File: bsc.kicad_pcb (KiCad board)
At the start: 4 copper layers, 120 x 100 mm, 278 parts, among them IC1 ILD217T, IC2 ILD217T, IC3 ILD217T, J1 Conn_JTAG_ESP, J10 JP_REL1_COM_12V, J12 JP_REL2_COM_12V, J13 JP_REL3_COM_12V, J14 Conn_REL1, J15 Conn_REL2, J16 Conn_REL3, J2 Prog, J3 Conn_Extension, J4 Boot, J5 JP_REL4_COM_12V, J6 JP_U3TX_EN, J8 JP_REL5_COM_12V, J9 JP_REL6_COM_12V, K2 TIANBO-HJR-4102-L, K3 TIANBO-HJR-4102-L, K4 TIANBO-HJR-4102-L, K5 TIANBO-HJR-4102-L, K6 TIANBO-HJR-4102-L, K7 TIANBO-HJR-4102-L, Q1 BC857BS, Q10 BC846, Q11 BC846, Q12 IRLML2244, Q13 BC857BS, Q14 IRLML2244, Q2 BSS138, Q3 BSS138, Q4 BSS138, Q5 BSS138, Q6 BSS138, Q7 BSS138, Q8 BC846, Q9 BC846, U1 LMO78_03-0.5, U10 74HC595, U11 74HC14, U12 74HC165, U13 ADuM1201AR, U16 SP3485EN, U19 LMO78_05-0.5, U2 ESP32WROOM32E16, U20 HC 151, U3 ADM2483xRW, U4 ADuM1201AR, U6 ADuM1201AR, U7 SN65HVD234, U8 SP3485EN, X1 Conn_S2, X2 Conn_S1, X3 Conn_DI, X4 Conn_SV, X5 Conn_Rel2, X6 Conn_Rel1

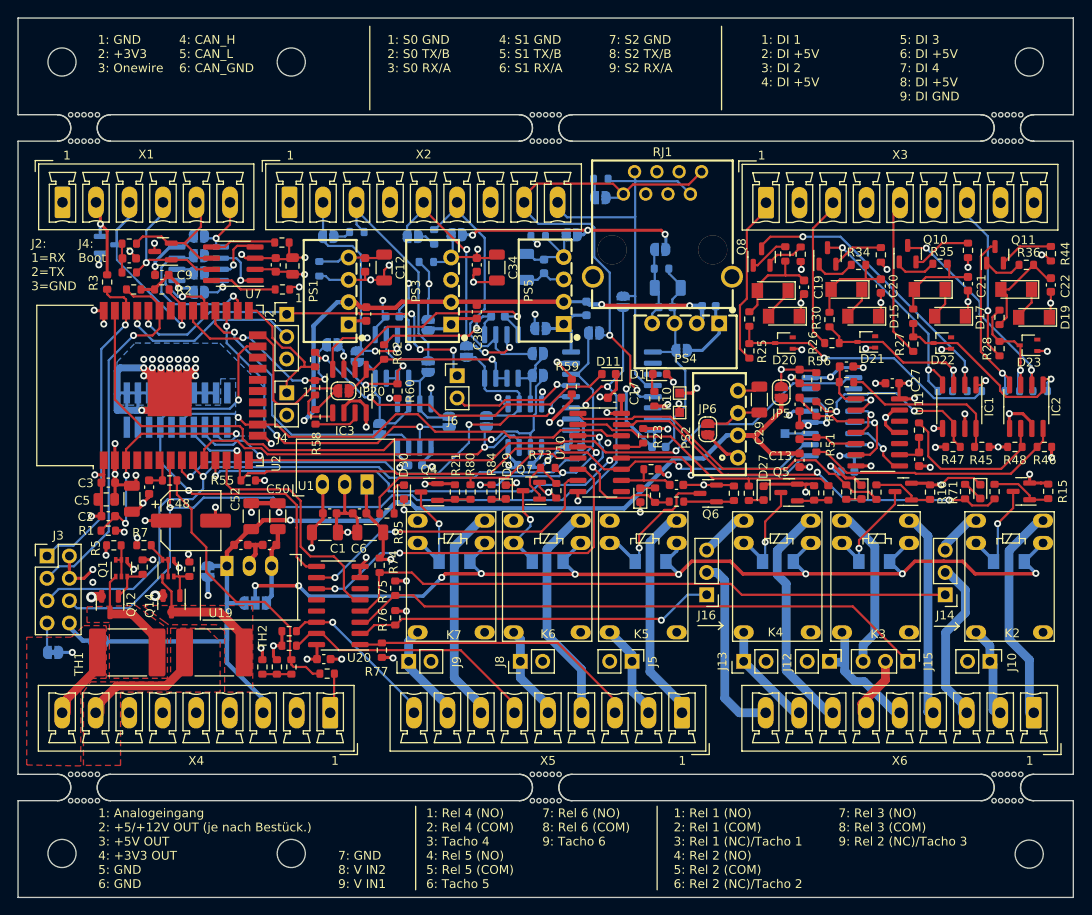
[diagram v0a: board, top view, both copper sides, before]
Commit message: Improvements added (Ref 2.4.1)
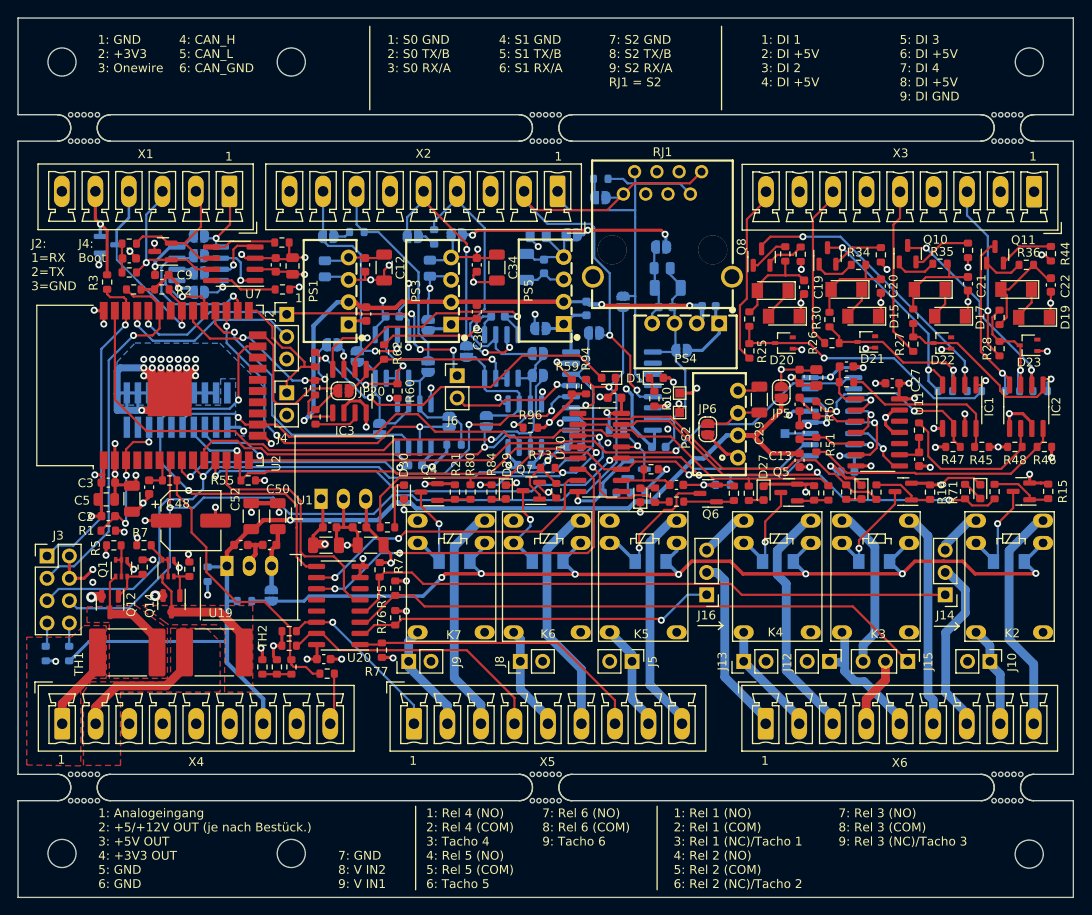
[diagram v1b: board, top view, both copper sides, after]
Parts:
- removed JP28: 12V_5V, Jumper:SolderJumper-2_P1.3mm_Bridged_RoundedPad1.0x1.5mm
- removed JP29: JP_REL_VCC, Jumper:SolderJumper-3_P1.3mm_Bridged12_RoundedPad1.0x1.5mm_NumberLabels
- removed JP30: JP_EXT_5V, Jumper:SolderJumper-2_P1.3mm_Bridged_RoundedPad1.0x1.5mm
- removed JP31: JP_EXT_3V3, Jumper:SolderJumper-2_P1.3mm_Bridged_RoundedPad1.0x1.5mm
- added C36: 10uF, Capacitor_SMD:C_0603_1608Metric, B.Cu at (97.3, 70.0)
- added JP25: REL_VIN, Jumper:SolderJumper-2_P1.3mm_Open_RoundedPad1.0x1.5mm, B.Cu at (58.8, 81.7)
- added Q15: BSS138, Package_TO_SOT_SMD:SOT-23, B.Cu at (100.3, 67.3)
- added R61: 0R, Resistor_SMD:R_0603_1608Metric, B.Cu at (51.6, 79.2)
- added R86: 0R, Resistor_SMD:R_0603_1608Metric, B.Cu at (33.1, 88.3)
- added R87: 0R, Resistor_SMD:R_0603_1608Metric, B.Cu at (35.8, 88.3)
- added R91: 0R, Resistor_SMD:R_0603_1608Metric, B.Cu at (55.8, 82.3)
- added R92: 10k, Resistor_SMD:R_0603_1608Metric, B.Cu at (110.2, 69.1)
- added R93: 100k, Resistor_SMD:R_0603_1608Metric, B.Cu at (100.5, 70.0)
- added R94: 10k, Resistor_SMD:R_0603_1608Metric, F.Cu at (94.6, 57.9)
- added R95: 10k, Resistor_SMD:R_0603_1608Metric, B.Cu at (79.6, 64.5)
- added R96: 10k, Resistor_SMD:R_0603_1608Metric, F.Cu at (88.3, 62.6)
- C10, C13, C30, C31, C38: value 100n -> 10uF
- C12, C29, C34, C35, C42: value 22µ/10V -> 10uF/10V
- PS2: value B0505S-1WR2_C909796 -> B0505S-1WR2
- R19, R56, R63, R64, R65: value 330R -> 220R; footprint Resistor_SMD:R_0603_1608Metric -> Resistor_SMD:R_0805_2012Metric
- R23: moved to B.Cu
- U1: value LMO78_03-0.5 -> K7803-1000R3
- moved X1 19.0 mm to (54.0, 35.7), turned to 180 degrees
- moved R23 3.11 mm to (98.0, 62.9), turned to 180 degrees
- moved U1 1.64 mm to (66.8, 70.6)
- moved C7 1.59 mm to (65.4, 73.9)
- moved C8 1.59 mm to (68.8, 73.9)
- moved R85 1.58 mm to (72.0, 73.9)
- moved C1 1.45 mm to (65.0, 75.9)
- moved C6 1.45 mm to (70.1, 75.9)
- moved X2 1.25 mm to (76.1, 35.7), turned to 180 degrees
- moved X3 1.25 mm to (130.3, 35.8), turned to 180 degrees
- moved X4 1.25 mm to (50.3, 96.2), turned to 0 degrees
- moved X5 1.25 mm to (90.3, 96.2), turned to 0 degrees
- moved X6 1.25 mm to (130.3, 96.2), turned to 0 degrees
- moved R63 0.82 mm to (76.8, 44.5), turned to 90 degrees
- moved R19 0.64 mm to (64.9, 44.5)
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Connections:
- J1 pad 1: unconnected-(J1-Pad1) -> +3V3
- J1 pad 15: unconnected-(J1-Pad15) -> /RST_ESP
- J1 pad 3: /RST_ESP -> unconnected-(J1-Pin_3-Pad3)
- R23 pad 1: GND -> Net-(Q15-D)
- R23 pad 2: Net-(R23-Pad2) -> +3V3
- U10 pad 13: Net-(R23-Pad2) -> Net-(Q15-D)
- X1 pad 1: GND -> /CAN_GND
- X1 pad 2: +3V3 -> /CAN_L
- X1 pad 3: /onewire -> /CAN_H
- X1 pad 4: /CAN_H -> /onewire
- X1 pad 5: /CAN_L -> +3V3
- X1 pad 6: /CAN_GND -> GND
- X2 pad 1: /serial/U1_GND -> /serial/U3RX_O
- X2 pad 2: /serial/U1TX_O -> /serial/U3TX_O
- X2 pad 3: /serial/U1RX_O -> /serial/U3_GND
- X2 pad 4: /serial/U2_GND -> /serial/U2RX_O
- X2 pad 6: /serial/U2RX_O -> /serial/U2_GND
- X2 pad 7: /serial/U3_GND -> /serial/U1RX_O
- X2 pad 8: /serial/U3TX_O -> /serial/U1TX_O
- X2 pad 9: /serial/U3RX_O -> /serial/U1_GND
- X3 pad 1: /INPUT/DI1_P -> GND1
- X3 pad 3: /INPUT/DI2_P -> /INPUT/DI4_P
- X3 pad 7: /INPUT/DI4_P -> /INPUT/DI2_P
- X3 pad 9: GND1 -> /INPUT/DI1_P
- X4 pad 1: /AI1 -> V_IN1
- X4 pad 2: V_IN -> V_IN2
- X4 pad 3: +5V -> GND
- X4 pad 4: +3V3 -> GND
- X4 pad 6: GND -> +3V3
- X4 pad 7: GND -> +5V
- X4 pad 8: V_IN2 -> V_IN
- X4 pad 9: V_IN1 -> /AI1
- X5 pad 1: /OUTPUT/REL4_NO -> /OUTPUT/TACHO6
- X5 pad 2: /OUTPUT/REL4_COM -> /OUTPUT/REL6_COM
- X5 pad 3: /OUTPUT/TACHO4 -> /OUTPUT/REL6_NO
- X5 pad 4: /OUTPUT/REL5_NO -> /OUTPUT/TACHO5
- X5 pad 6: /OUTPUT/TACHO5 -> /OUTPUT/REL5_NO
- X5 pad 7: /OUTPUT/REL6_NO -> /OUTPUT/TACHO4
- X5 pad 8: /OUTPUT/REL6_COM -> /OUTPUT/REL4_COM
- X5 pad 9: /OUTPUT/TACHO6 -> /OUTPUT/REL4_NO
- X6 pad 1: /OUTPUT/REL1_NO -> /OUTPUT/REL3_NC_TACHO
- X6 pad 2: /OUTPUT/REL1_COM -> /OUTPUT/REL3_COM
- X6 pad 3: /OUTPUT/REL1_NC_TACHO -> /OUTPUT/REL3_NO
- X6 pad 4: /OUTPUT/REL2_NO -> /OUTPUT/REL2_NC_TACHO
- X6 pad 6: /OUTPUT/REL2_NC_TACHO -> /OUTPUT/REL2_NO
- X6 pad 7: /OUTPUT/REL3_NO -> /OUTPUT/REL1_NC_TACHO
- X6 pad 8: /OUTPUT/REL3_COM -> /OUTPUT/REL1_COM
- X6 pad 9: /OUTPUT/REL3_NC_TACHO -> /OUTPUT/REL1_NO
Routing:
- net +3V3: track 172.1 -> 188.8 mm, vias 32 -> 33
- net /RST_ESP: track 29.4 -> 16.9 mm
- net Net-(Q15-D): track 0.00 -> 7.31 mm, vias 0 -> 1
- net /serial/U2RX_S: track 7.44 -> 12.1 mm, vias 0 -> 1
- net GND: track 364.3 -> 368.6 mm
- net /serial/U1RX_S: track 9.99 -> 14.0 mm
- net Net-(Q15-G): track 0.00 -> 3.41 mm
- net +5V: track 191.5 -> 194.8 mm
- net /U3RX: track 104.3 -> 107.0 mm
- net Net-(R23-Pad2): track 2.66 -> 0.00 mm
- net /OUTPUT/VCC_REL: track 124.0 -> 122.1 mm, vias 9 -> 7
- net Net-(D30-A): track 4.12 -> 5.67 mm
- net /OUTPUT/REL6: track 27.5 -> 29.0 mm
- net /serial/U1RX_O: track 32.2 -> 30.7 mm
- net /INPUT/DI3_P: track 18.0 -> 19.4 mm
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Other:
- board text added: "7: Rel 3 (NO) 8: Rel 3 (COM) 9: Rel 3 (NC)/Tacho 3"
- board text added: "7: S2 GND 8: S2 TX/B 9: S2 RX/A RJ1 = S2"
- board text added: "JP25+R91 = Config. VCC REL: R91: +5V OR JP25: V_IN"
- board text added: "PCB V2.4.1 https://github.com/shining-man/bsc_hw"
- board text added: "R61: V_IN -> +5V"
- board text added: "R86: 3V3 to Ext.-Port R87: 5V to Ext.-Port"
- board text removed: "7: Rel 3 (NO) 8: Rel 3 (COM) 9: Rel 2 (NC)/Tacho 3"
- board text removed: "7: S2 GND 8: S2 TX/B 9: S2 RX/A"
- board text removed: "JP28: V_IN -> +5V"
- board text removed: "JP29 VCC REL: 1-2: +5V | 2-3: V_IN"
- board text removed: "JP30: 5V to Ext.-Port JP31: 3V3 to Ext.-Port"
- board text removed: "PCB V2.4"

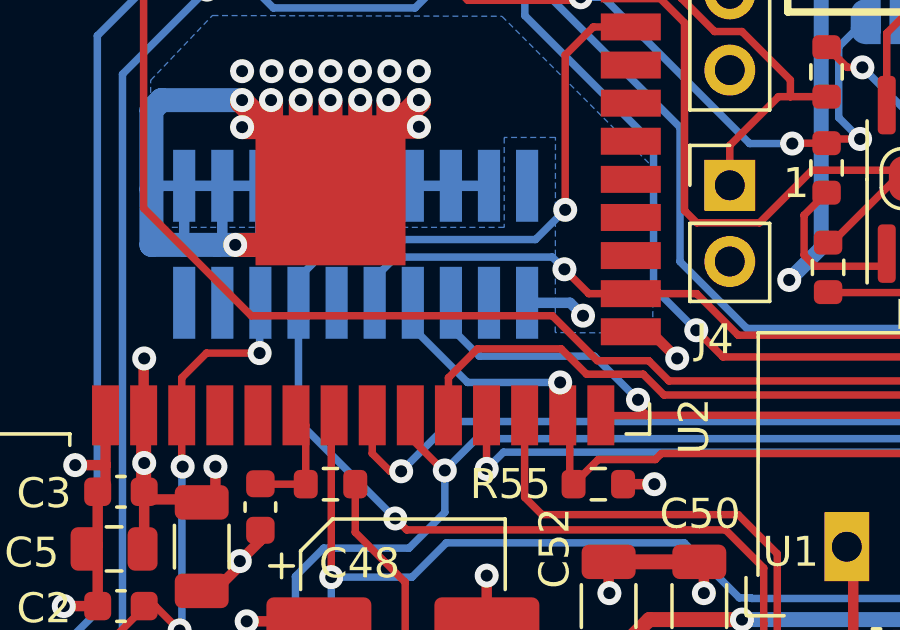
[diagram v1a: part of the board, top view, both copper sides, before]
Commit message: Track spacing in layout corrected
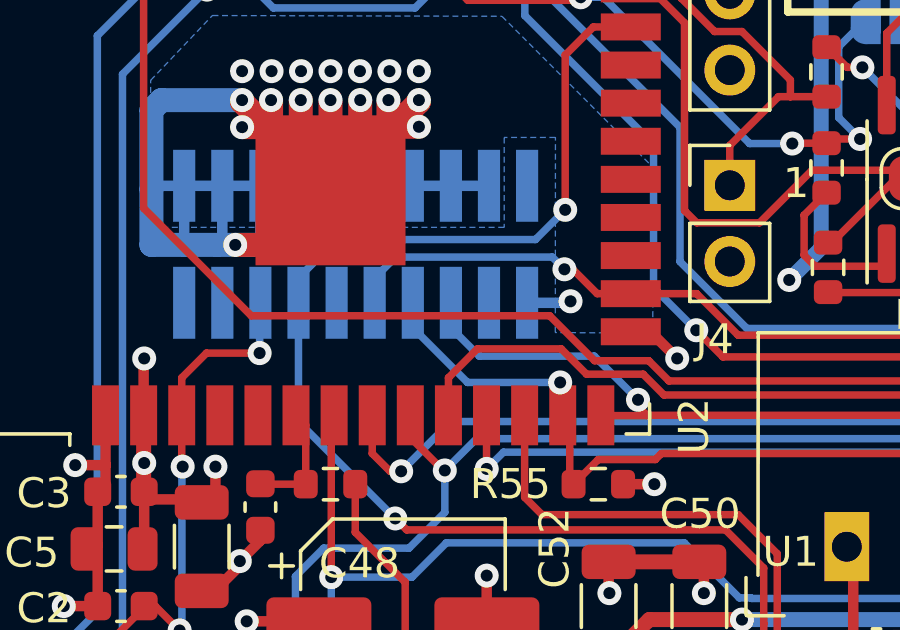
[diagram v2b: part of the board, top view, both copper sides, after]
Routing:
- net +3V3: track 188.8 -> 188.2 mm
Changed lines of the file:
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@@
   (via (at 81.6864 40.6908) (size 0.8) (drill 0.4) (layers "F.Cu" "B.Cu") (net 39))
   (via (at 39.37 39.4208) (size 0.8) (drill 0.4) (layers "F.Cu" "B.Cu") (net 39))
-  (via (at 55.661681 62.964129) (size 0.8) (drill 0.4) (layers "F.Cu" "B.Cu") (net 39))
+  (via (at 55.245 62.484) (size 0.8) (drill 0.4) (layers "F.Cu" "B.Cu") (net 39))
   (via (at 131.953 59.2195) (size 0.8) (drill 0.4) (layers "F.Cu" "B.Cu") (net 39))
   (via (at 134.3152 64.8208) (size 0.8) (drill 0.4) (layers "F.Cu" "B.Cu") (net 39))
@@
   (segment (start 94.2848 40.64) (end 94.7928 40.132) (width 0.35) (layer "B.Cu") (net 39))
   (segment (start 78.7532 65.355881) (end 77.090581 67.0185) (width 0.35) (layer "B.Cu") (net 39))
-  (segment (start 55.232352 62.5348) (end 55.661681 62.964129) (width 0.35) (layer "B.Cu") (net 39))
   (segment (start 92.443 64.77) (end 91.935 64.77) (width 0.35) (layer "B.Cu") (net 39))
   (segment (start 48.071 46.541691) (end 48.234955 46.705646) (width 0.35) (layer "B.Cu") (net 39))
+  (segment (start 53.7972 62.5348) (end 55.1942 62.5348) (width 0.35) (layer "B.Cu") (net 39))
   (segment (start 92.443 64.77) (end 91.7702 64.77) (width 0.35) (layer "B.Cu") (net 39))
   (segment (start 78.7532 64.516) (end 78.7532 65.355881) (width 0.35) (layer "B.Cu") (net 39))
@@
   (segment (start 91.7702 64.77) (end 90.2462 66.294) (width 0.35) (layer "B.Cu") (net 39))
   (segment (start 76.962 64.832) (end 76.962 65.6082) (width 0.35) (layer "B.Cu") (net 39))
-  (segment (start 53.7972 62.5348) (end 55.232352 62.5348) (width 0.35) (layer "B.Cu") (net 39))
   (segment (start 76.0606 66.9798) (end 77.051881 66.9798) (width 0.35) (layer "B.Cu") (net 39))
   (segment (start 76.962 65.6082) (end 75.9336 66.6366) (width 0.35) (layer "B.Cu") (net 39))
+  (segment (start 55.1942 62.5348) (end 55.245 62.484) (width 0.35) (layer "B.Cu") (net 39))
   (segment (start 123.444 65.786) (end 125.03 65.786) (width 0.35) (layer "B.Cu") (net 39))
   (segment (start 101.282 69.787) (end 103.759 67.31) (width 0.35) (layer "B.Cu") (net 39))
@@
   (segment (start 107.850824 62.1792) (end 113.5123 62.1792) (width 0.25) (layer "B.Cu") (net 51))
   (segment (start 123.7129 57.5415) (end 124.3584 56.896) (width 0.25) (layer "B.Cu") (net 51))
+  (segment (start 56.134 62.23) (end 55.3212 61.4172) (width 0.25) (layer "F.Cu") (net 52))
   (segment (start 91.6835 62.8755) (end 96.3527 62.8755) (width 0.25) (layer "F.Cu") (net 52))
   (segment (start 75.453131 61.051331) (end 77.4446 63.0428) (width 0.25) (layer "F.Cu") (net 52))
@@
   (segment (start 96.9772 63.5) (end 98.614 63.5) (width 0.25) (layer "F.Cu") (net 52))
   (segment (start 60.831823 63.613699) (end 70.401563 63.613699) (width 0.25) (layer "F.Cu") (net 52))
-  (segment (start 57.255 62.23) (end 55.8546 62.23) (width 0.25) (layer "F.Cu") (net 52))
   (segment (start 96.3527 62.8755) (end 96.9772 63.5) (width 0.25) (layer "F.Cu") (net 52))
   (segment (start 85.2678 63.0428) (end 85.920511 63.695511) (width 0.25) (layer "F.Cu") (net 52))
+  (segment (start 55.3212 61.4172) (end 55.0418 61.4172) (width 0.25) (layer "F.Cu") (net 52))
   (segment (start 70.401563 63.613699) (end 72.963931 61.051331) (width 0.25) (layer "F.Cu") (net 52))
   (segment (start 90.863489 63.695511) (end 91.6835 62.8755) (width 0.25) (layer "F.Cu") (net 52))
+  (segment (start 57.255 62.23) (end 56.134 62.23) (width 0.25) (layer "F.Cu") (net 52))
   (segment (start 72.963931 61.051331) (end 75.453131 61.051331) (width 0.25) (layer "F.Cu") (net 52))
-  (segment (start 55.8546 62.23) (end 55.0418 61.4172) (width 0.25) (layer "F.Cu") (net 52))
   (segment (start 59.448124 62.23) (end 60.831823 63.613699) (width 0.25) (layer "F.Cu") (net 52))
   (segment (start 57.255 62.23) (end 59.448124 62.23) (width 0.25) (layer "F.Cu") (net 52))
@@
   (segment (start 47.4472 44.577) (end 46.77148 45.25272) (width 0.25) (layer "B.Cu") (net 60))
   (segment (start 46.77148 45.25272) (end 46.77148 46.27208) (width 0.25) (layer "B.Cu") (net 60))
-  (segment (start 56.138784 64.4652) (end 57.8526 64.4652) (width 0.25) (layer "F.Cu") (net 61))
+  (segment (start 41.015 59.3792) (end 44.6024 62.9666) (width 0.25) (layer "F.Cu") (net 61))
+  (segment (start 41.015 49.285) (end 41.015 59.3792) (width 0.25) (layer "F.Cu") (net 61))
+  (segment (start 54.548892 62.9666) (end 56.047492 64.4652) (width 0.25) (layer "F.Cu") (net 61))
+  (segment (start 44.6024 62.9666) (end 54.548892 62.9666) (width 0.25) (layer "F.Cu") (net 61))
+  (segment (start 57.8526 64.4652) (end 58.526301 65.138901) (width 0.25) (layer "F.Cu") (net 61))
+  (segment (start 72.7964 63.9318) (end 83.82 63.9318) (width 0.25) (layer "F.Cu") (net 61))
+  (segment (start 71.589299 65.138901) (end 72.7964 63.9318) (width 0.25) (layer "F.Cu") (net 61))
+  (segment (start 56.047492 64.4652) (end 57.8526 64.4652) (width 0.25) (layer "F.Cu") (net 61))
   (segment (start 58.526301 65.138901) (end 71.589299 65.138901) (width 0.25) (layer "F.Cu") (net 61))
-  (segment (start 54.640184 62.9666) (end 56.138784 64.4652) (width 0.25) (layer "F.Cu") (net 61))
-  (segment (start 41.015 59.3792) (end 44.6024 62.9666) (width 0.25) (layer "F.Cu") (net 61))
-  (segment (start 57.8526 64.4652) (end 58.526301 65.138901) (width 0.25) (layer "F.Cu") (net 61))
-  (segment (start 44.6024 62.9666) (end 54.640184 62.9666) (width 0.25) (layer "F.Cu") (net 61))
-  (segment (start 71.589299 65.138901) (end 72.7964 63.9318) (width 0.25) (layer "F.Cu") (net 61))
-  (segment (start 72.7964 63.9318) (end 83.82 63.9318) (width 0.25) (layer "F.Cu") (net 61))
-  (segment (start 41.015 49.285) (end 41.015 59.3792) (width 0.25) (layer "F.Cu") (net 61))
   (via (at 83.82 63.9318) (size 0.8) (drill 0.4) (layers "F.Cu" "B.Cu") (net 61))
   (segment (start 88.646 62.8396) (end 88.265 63.2206) (width 0.25) (layer "B.Cu") (net 61))
